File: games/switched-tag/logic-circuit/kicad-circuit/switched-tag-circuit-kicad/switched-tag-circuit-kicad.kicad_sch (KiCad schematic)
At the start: 0 parts

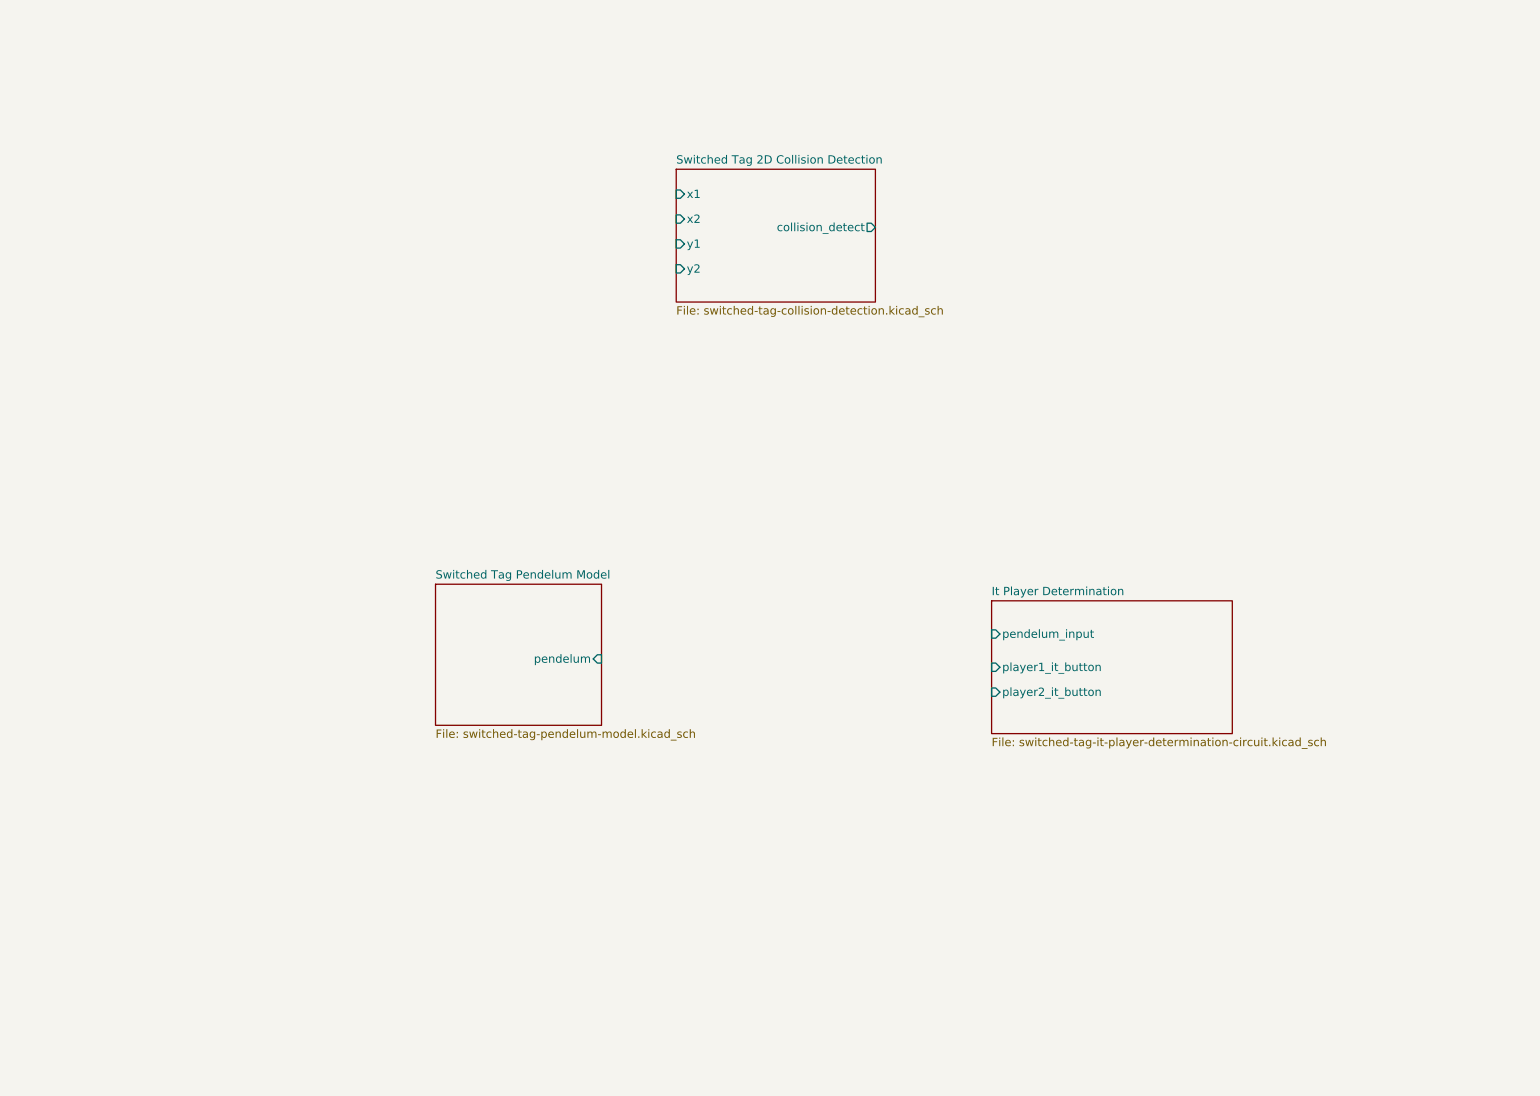
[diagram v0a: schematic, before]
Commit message: Saving progress on kicad schematic. Trying to set up ngspice simulation.
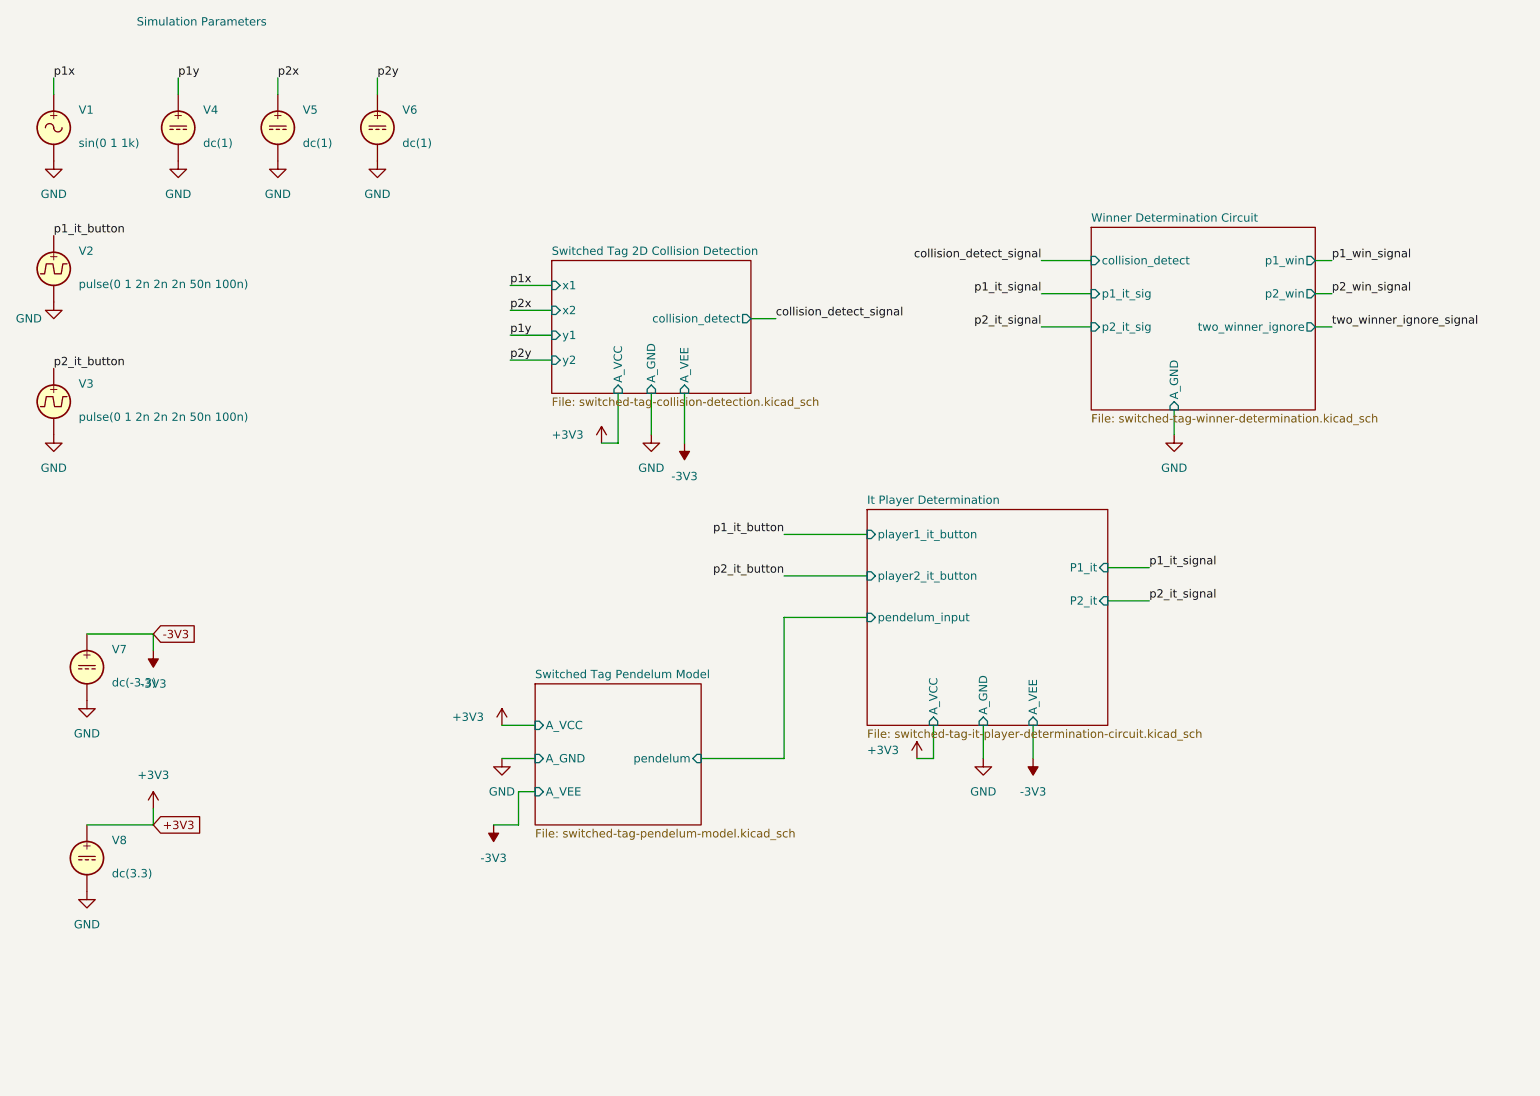
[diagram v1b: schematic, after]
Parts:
- added V1: (no value), symbol Simulation_SPICE:VSIN
- added V2, V3: (no value), symbol Simulation_SPICE:VPULSE
- added V4, V5, V6, V7, V8: (no value), symbol Simulation_SPICE:VDC
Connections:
- new net +3V3: V8.1
- new net -3V3: V7.1
- new net GND: V1.2, V2.2, V3.2, V4.2, V5.2, V6.2, V7.2, V8.2
- new net p1_it_button: V2.1
- new net p1x: V1.1
- new net p1y: V4.1
- new net p2_it_button: V3.1
- new net p2x: V5.1
- new net p2y: V6.1
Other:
- added sheet Winner Determination Circuit (switched-tag-winner-determination.kicad_sch)
- sheet It Player Determination  ports: added A_GND, A_VCC, A_VEE, P1_it, P2_it; removed none
- sheet Switched Tag 2D Collision Detection ports: added A_GND, A_VCC, A_VEE; removed none
- sheet Switched Tag Pendelum Model ports: added A_GND, A_VCC, A_VEE; removed none
- note added: "Simulation Parameters"

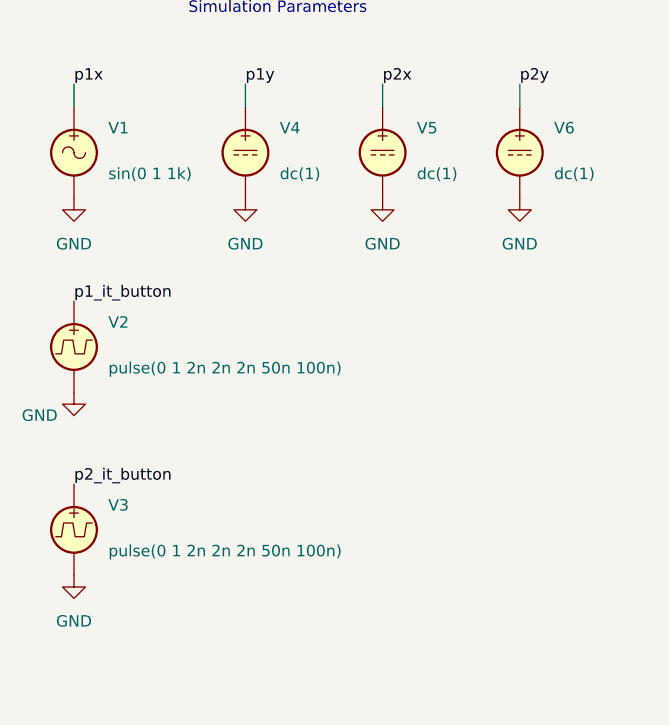
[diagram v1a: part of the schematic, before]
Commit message: Have kicad simulation working. Need to debug pendelum of kicad circuit and it player determination.
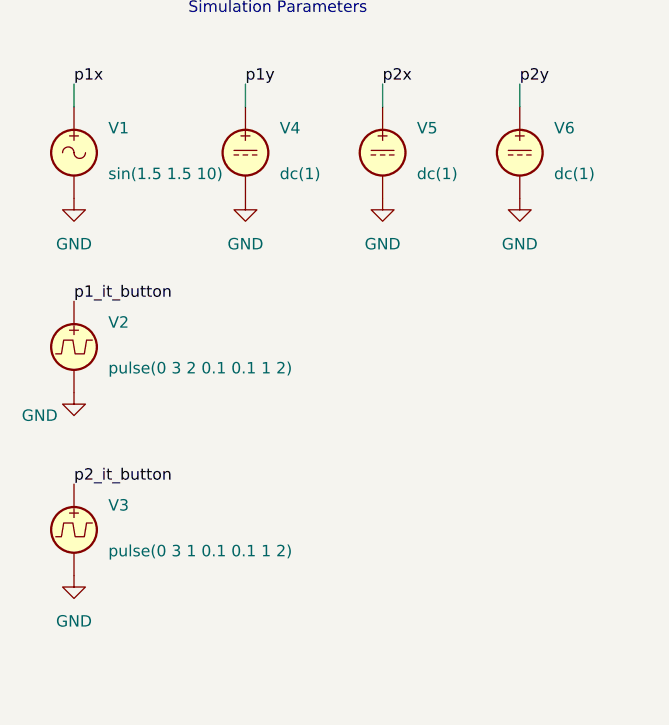
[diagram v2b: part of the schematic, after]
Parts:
- V1: Spice_Model sin(0 1 1k) -> sin(1.5 1.5 10)
- V2: Spice_Model pulse(0 1 2n 2n 2n 50n 100n) -> pulse(0 3 2 0.1 0.1 1 2)
- V3: Spice_Model pulse(0 1 2n 2n 2n 50n 100n) -> pulse(0 3 1 0.1 0.1 1 2)
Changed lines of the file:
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@@
       (effects (font (size 1.27 1.27)) (justify left) hide)
     )
-    (property "Spice_Model" "pulse(0 1 2n 2n 2n 50n 100n)" (id 6) (at 29.21 79.8201 0)
+    (property "Spice_Model" "pulse(0 3 1 0.1 0.1 1 2)" (id 6) (at 29.21 79.8201 0)
       (effects (font (size 1.27 1.27)) (justify left))
     )
@@
       (effects (font (size 1.27 1.27)) (justify left) hide)
     )
-    (property "Spice_Model" "pulse(0 1 2n 2n 2n 50n 100n)" (id 6) (at 29.21 59.5001 0)
+    (property "Spice_Model" "pulse(0 3 2 0.1 0.1 1 2)" (id 6) (at 29.21 59.5001 0)
       (effects (font (size 1.27 1.27)) (justify left))
     )
@@
       (effects (font (size 1.27 1.27)) (justify left) hide)
     )
-    (property "Spice_Model" "sin(0 1 1k)" (id 6) (at 29.21 37.9101 0)
-      (effects (font (size 1.27 1.27)) (justify left))
-    )
+    (property "Spice_Model" "sin(1.5 1.5 10)" (id 6) (at 29.21 37.9101 0)
+      (effects (font (size 1.27 1.27)) (justify left))
+    )

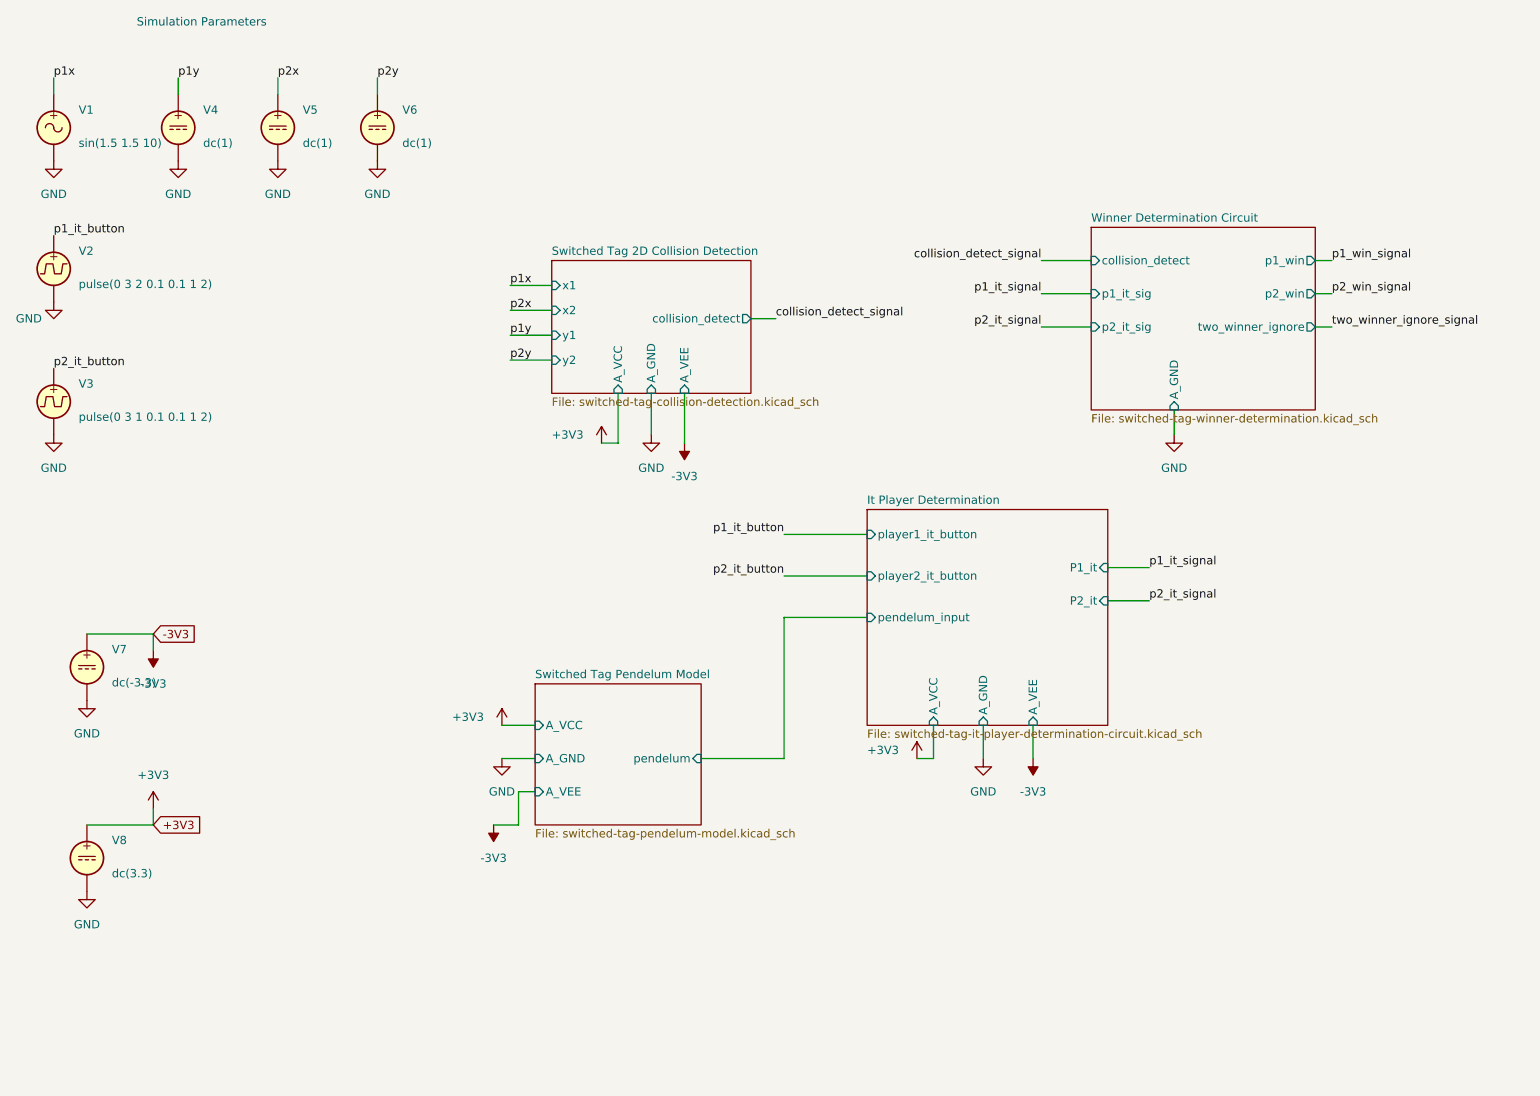
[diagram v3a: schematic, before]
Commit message: Changed spice model of opamp in kicad sim. Fixed design error in it player determination in ltspice and kicad schematic
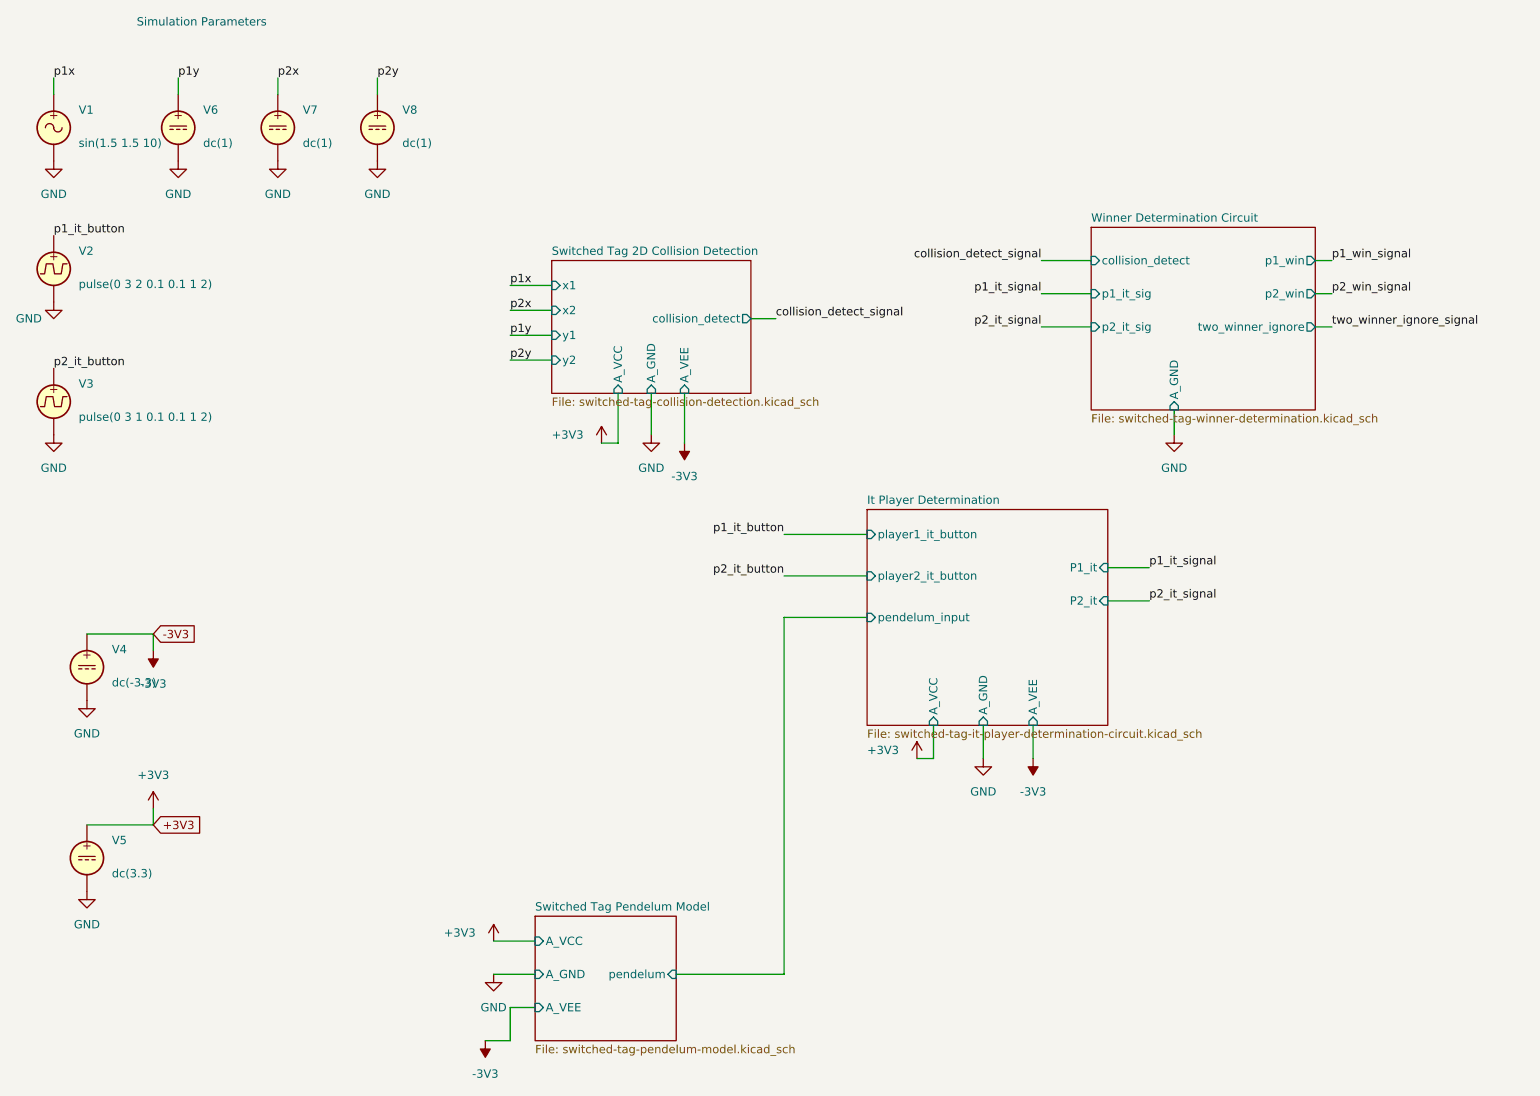
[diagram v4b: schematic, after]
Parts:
- renumbered V7 to V4, V8 to V5, V4 to V6, V5 to V7, V6 to V8
